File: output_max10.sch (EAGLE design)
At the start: 56 parts, among them IC4 IS61WV1288EEBLL-10HLI, IC5 10M04EQFP144

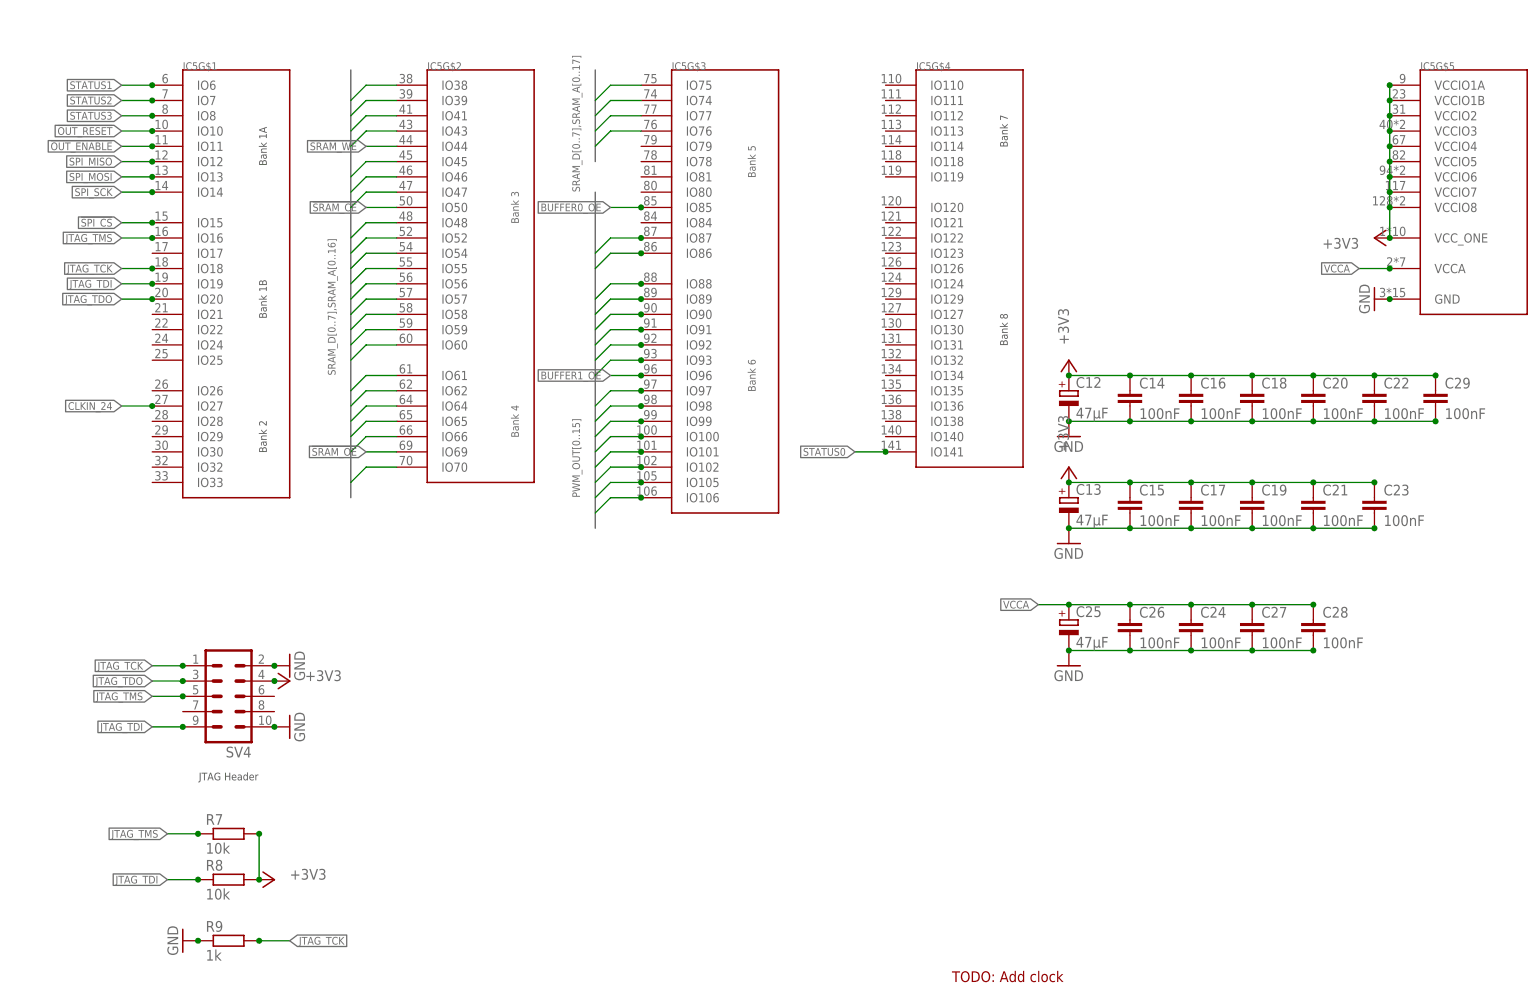
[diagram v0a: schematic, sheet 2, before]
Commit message: Added clock generator to FPGA (lol)
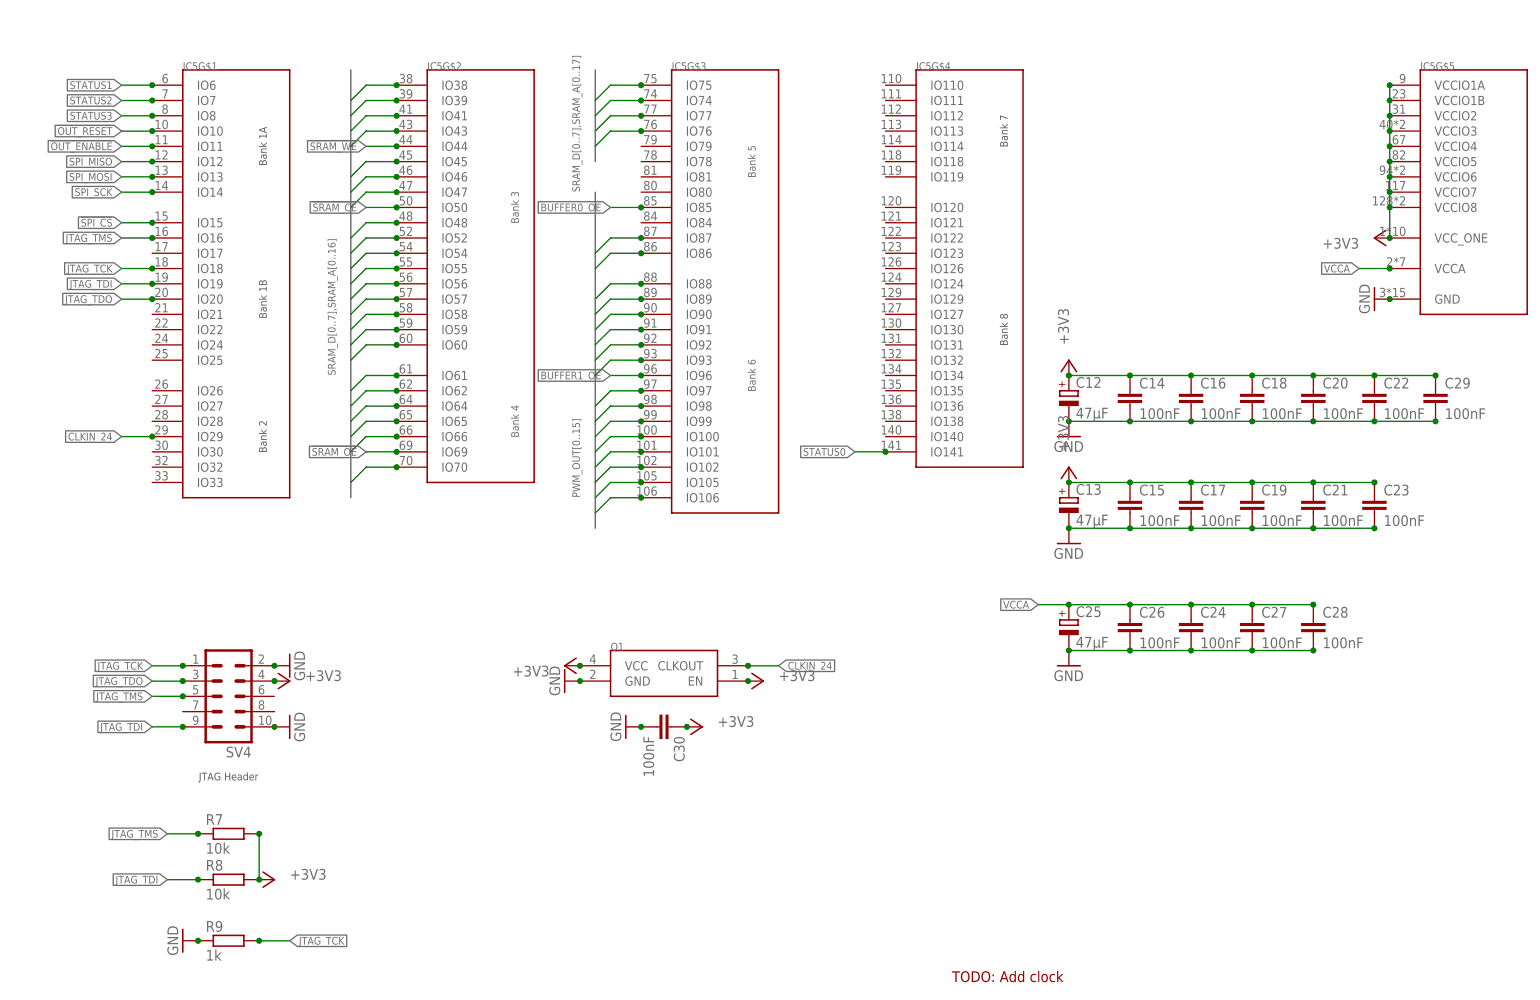
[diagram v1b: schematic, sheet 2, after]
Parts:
- added C30: 100nF, rcl:C-EUC0805
- added Q1: (no value), lichtenstein_onion:DSC61XX
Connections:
- net +3V3: now also C30.1, Q1.EN, Q1.VCC
- net CLKIN_24: now also IC5G$1.IO29, Q1.CLKOUT; no longer IC5G$1.IO27
- net GND: now also C30.2, Q1.GND

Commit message: BOM for base board
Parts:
- IC4: MOUSER (none) -> 870-61WV1288ELL10HLI
- Q1: MOUSER (none) -> 579-6101JI2A0240000T
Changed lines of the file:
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@@
 <part name="+3V32" library="supply1" library_urn="urn:adsk.eagle:library:371" deviceset="+3V3" device=""/>
 <part name="GND4" library="supply1" library_urn="urn:adsk.eagle:library:371" deviceset="GND" device=""/>
-<part name="IC4" library="lichtenstein_onion" deviceset="IS61WV1288EEBLL" device="TSOP32-I" value="IS61WV1288EEBLL-10HLI"/>
+<part name="IC4" library="lichtenstein_onion" deviceset="IS61WV1288EEBLL" device="TSOP32-I" value="IS61WV1288EEBLL-10HLI">
+<attribute name="MOUSER" value="870-61WV1288ELL10HLI"/>
+</part>
 <part name="C10" library="rcl" library_urn="urn:adsk.eagle:library:334" deviceset="C-EU" device="C0805" package3d_urn="urn:adsk.eagle:package:23617/2" value="100nF">
 <attribute name="MOUSER" value="710-885012207072"/>
@@
 <attribute name="MOUSER" value="710-885012207072"/>
 </part>
-<part name="Q1" library="lichtenstein_onion" deviceset="DSC61XX" device=""/>
+<part name="Q1" library="lichtenstein_onion" deviceset="DSC61XX" device="">
+<attribute name="MOUSER" value="579-6101JI2A0240000T"/>
+</part>
 <part name="+3V3" library="supply1" library_urn="urn:adsk.eagle:library:371" deviceset="+3V3" device=""/>
 <part name="GND21" library="supply1" library_urn="urn:adsk.eagle:library:371" deviceset="GND" device=""/>
@@
 </instance>
 <instance part="GND4" gate="1" x="38.1" y="154.94" rot="R90"/>
-<instance part="IC4" gate="G$1" x="190.5" y="99.06"/>
+<instance part="IC4" gate="G$1" x="190.5" y="99.06">
+<attribute name="MOUSER" x="190.5" y="99.06" size="1.27" layer="96" display="off"/>
+</instance>
 <instance part="C10" gate="G$1" x="203.2" y="111.76">
 <attribute name="MOUSER" x="203.2" y="111.76" size="1.27" layer="96" align="top-center" display="off"/>
@@
 <attribute name="MOUSER" x="231.14" y="129.54" size="1.27" layer="96" align="top-center" display="off"/>
 </instance>
-<instance part="Q1" gate="G$1" x="93.98" y="86.36"/>
+<instance part="Q1" gate="G$1" x="93.98" y="86.36">
+<attribute name="MOUSER" x="93.98" y="86.36" size="1.27" layer="96" display="off"/>
+</instance>
 <instance part="+3V3" gate="G$1" x="86.36" y="83.82" smashed="yes" rot="R90">
 <attribute name="VALUE" x="83.82" y="83.82" size="1.778" layer="96" rot="R180"/>

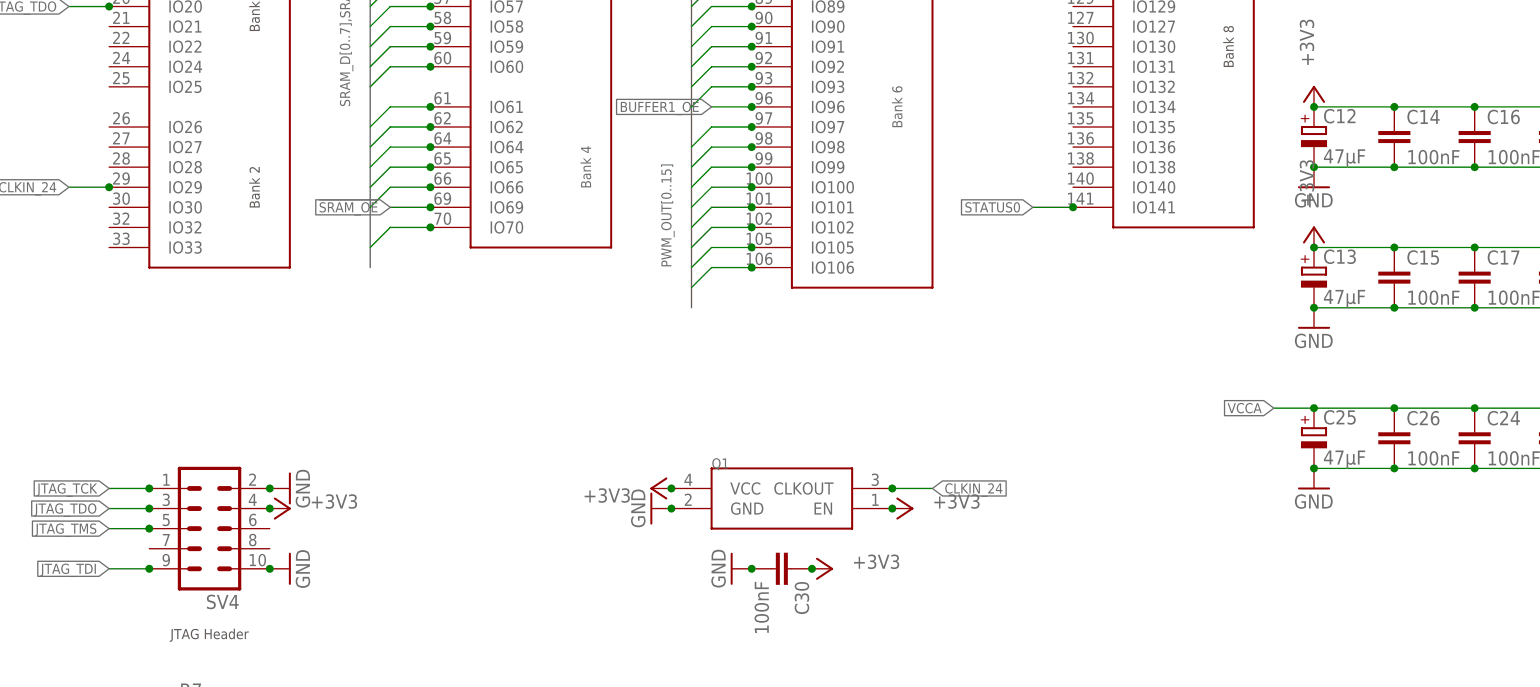
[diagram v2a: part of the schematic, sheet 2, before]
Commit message: Fixed some more footprints on MAX10 driver
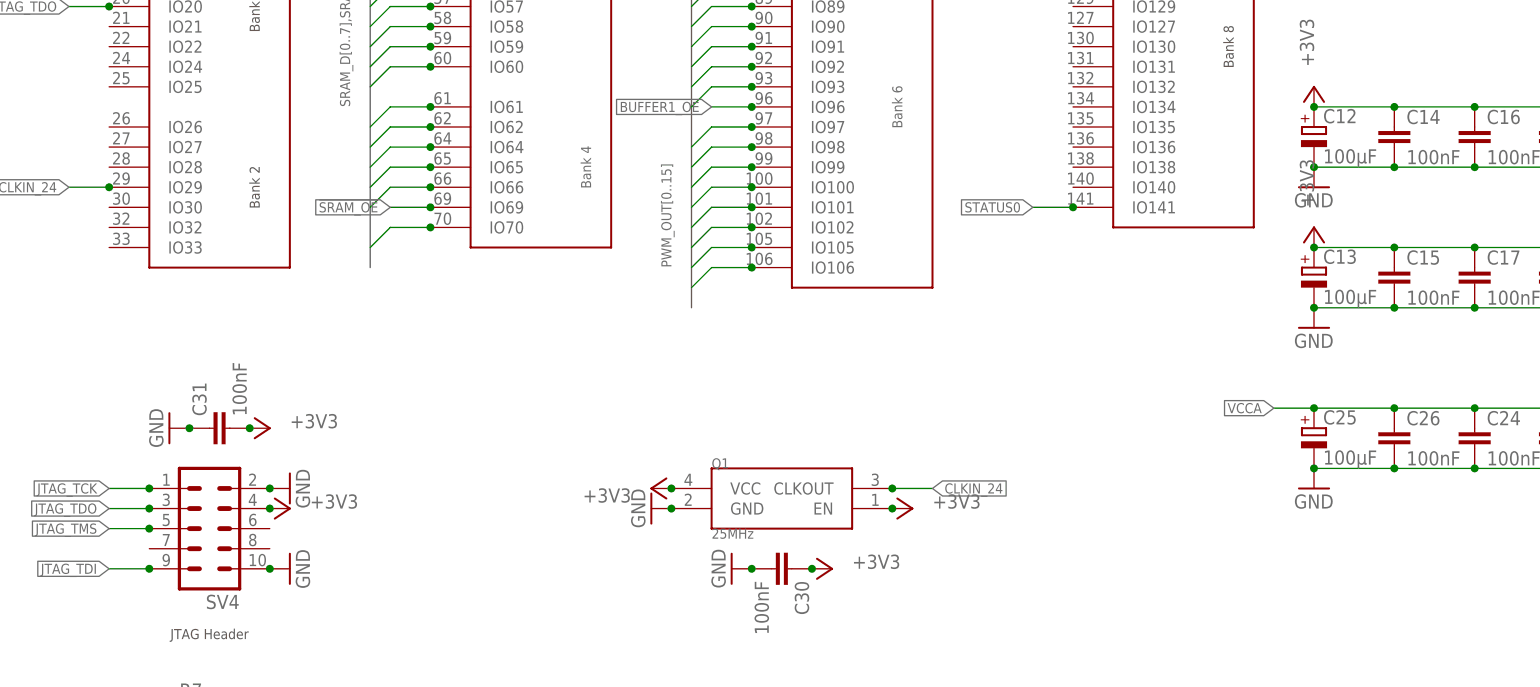
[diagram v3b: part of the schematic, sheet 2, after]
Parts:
- added C31: 100nF, rcl:C-EUC0805
- C12, C13, C25, C4, C9: value 47µF -> 100µF; device rcl:CPOL-EUCT6032 -> rcl:CPOL-EUSMCD
- Q1: value (none) -> 25MHz
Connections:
- net +3V3: now also C31.2
- net GND: now also C31.1
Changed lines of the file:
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@@
 <?xml version="1.0" encoding="utf-8"?>
 <!DOCTYPE eagle SYSTEM "eagle.dtd">
-<eagle version="8.7.0">
+<eagle version="9.0.1">
 <drawing>
 <settings>
@@
 <part name="GND7" library="supply1" library_urn="urn:adsk.eagle:library:371" deviceset="GND" device=""/>
 <part name="+3V34" library="supply1" library_urn="urn:adsk.eagle:library:371" deviceset="+3V3" device=""/>
-<part name="C4" library="rcl" library_urn="urn:adsk.eagle:library:334" deviceset="CPOL-EU" device="CT6032" package3d_urn="urn:adsk.eagle:package:23305/2" value="47µF">
+<part name="C4" library="rcl" library_urn="urn:adsk.eagle:library:334" deviceset="CPOL-EU" device="SMCD" package3d_urn="urn:adsk.eagle:package:23434/1" value="100µF">
 <attribute name="MOUSER" value="581-NOSD107M006"/>
 </part>
@@
 <part name="GND11" library="supply1" library_urn="urn:adsk.eagle:library:371" deviceset="GND" device=""/>
 <part name="+3V39" library="supply1" library_urn="urn:adsk.eagle:library:371" deviceset="+3V3" device=""/>
-<part name="C9" library="rcl" library_urn="urn:adsk.eagle:library:334" deviceset="CPOL-EU" device="CT6032" package3d_urn="urn:adsk.eagle:package:23305/2" value="47µF">
+<part name="C9" library="rcl" library_urn="urn:adsk.eagle:library:334" deviceset="CPOL-EU" device="SMCD" package3d_urn="urn:adsk.eagle:package:23434/1" value="100µF">
 <attribute name="MOUSER" value="581-NOSD107M006"/>
 </part>
@@
 <part name="GND14" library="supply1" library_urn="urn:adsk.eagle:library:371" deviceset="GND" device=""/>
 <part name="+3V312" library="supply1" library_urn="urn:adsk.eagle:library:371" deviceset="+3V3" device=""/>
-<part name="C12" library="rcl" library_urn="urn:adsk.eagle:library:334" deviceset="CPOL-EU" device="CT6032" package3d_urn="urn:adsk.eagle:package:23305/2" value="47µF">
+<part name="C12" library="rcl" library_urn="urn:adsk.eagle:library:334" deviceset="CPOL-EU" device="SMCD" package3d_urn="urn:adsk.eagle:package:23434/1" value="100µF">
 <attribute name="MOUSER" value="581-NOSD107M006"/>
 </part>
@@
 <part name="GND15" library="supply1" library_urn="urn:adsk.eagle:library:371" deviceset="GND" device=""/>
 <part name="+3V313" library="supply1" library_urn="urn:adsk.eagle:library:371" deviceset="+3V3" device=""/>
-<part name="C13" library="rcl" library_urn="urn:adsk.eagle:library:334" deviceset="CPOL-EU" device="CT6032" package3d_urn="urn:adsk.eagle:package:23305/2" value="47µF">
+<part name="C13" library="rcl" library_urn="urn:adsk.eagle:library:334" deviceset="CPOL-EU" device="SMCD" package3d_urn="urn:adsk.eagle:package:23434/1" value="100µF">
 <attribute name="MOUSER" value="581-NOSD107M006"/>
 </part>
@@
 </part>
 <part name="GND20" library="supply1" library_urn="urn:adsk.eagle:library:371" deviceset="GND" device=""/>
-<part name="C25" library="rcl" library_urn="urn:adsk.eagle:library:334" deviceset="CPOL-EU" device="CT6032" package3d_urn="urn:adsk.eagle:package:23305/2" value="47µF">
+<part name="C25" library="rcl" library_urn="urn:adsk.eagle:library:334" deviceset="CPOL-EU" device="SMCD" package3d_urn="urn:adsk.eagle:package:23434/1" value="100µF">
 <attribute name="MOUSER" value="581-NOSD107M006"/>
 </part>
@@
 <attribute name="MOUSER" value="710-885012207072"/>
 </part>
-<part name="Q1" library="lichtenstein_onion" deviceset="DSC61XX" device="">
+<part name="Q1" library="lichtenstein_onion" deviceset="DSC61XX" device="" value="25MHz">
 <attribute name="MOUSER" value="579-6101JI2A0240000T"/>
 </part>
@@
 <part name="+3V4" library="supply1" library_urn="urn:adsk.eagle:library:371" deviceset="+3V3" device=""/>
 <part name="+3V5" library="supply1" library_urn="urn:adsk.eagle:library:371" deviceset="+3V3" device=""/>
+<part name="C31" library="rcl" library_urn="urn:adsk.eagle:library:334" deviceset="C-EU" device="C0805" package3d_urn="urn:adsk.eagle:package:23617/2" value="100nF">
+<attribute name="MOUSER" value="710-885012207072"/>
+</part>
+<part name="GND23" library="supply1" library_urn="urn:adsk.eagle:library:371" deviceset="GND" device=""/>
+<part name="+3V6" library="supply1" library_urn="urn:adsk.eagle:library:371" deviceset="+3V3" device=""/>
 </parts>
 <sheets>
@@
 <attribute name="VALUE" x="121.92" y="81.28" size="1.778" layer="96"/>
 </instance>
+<instance part="C31" gate="G$1" x="30.48" y="91.44" rot="R90">
+<attribute name="MOUSER" x="30.48" y="91.44" size="1.27" layer="96" rot="R90" align="top-center" display="off"/>
+</instance>
+<instance part="GND23" gate="1" x="25.4" y="91.44" rot="R270"/>
+<instance part="+3V6" gate="G$1" x="38.1" y="91.44" smashed="yes" rot="R270">
+<attribute name="VALUE" x="40.64" y="91.44" size="1.778" layer="96"/>
+</instance>
 </instances>
 <busses>
@@
 <junction x="116.84" y="81.28"/>
 </segment>
+<segment>
+<pinref part="C31" gate="G$1" pin="2"/>
+<pinref part="+3V6" gate="G$1" pin="+3V3"/>
+<junction x="35.56" y="91.44"/>
+</segment>
 </net>
 <net name="GND" class="0">
@@
 <junction x="99.06" y="73.66"/>
 </segment>
-</net>
+<segment>
+<pinref part="C31" gate="G$1" pin="1"/>
+<pinref part="GND23" gate="1" pin="GND"/>
+<junction x="27.94" y="91.44"/>
+</segment>
+</net>
